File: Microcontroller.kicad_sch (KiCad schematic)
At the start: 17 parts, among them IC3 W25Q128JVSIQ, IC4 ESP32-S3R8, Q1 40MHz

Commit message: test 4
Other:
- note removed: "test text"
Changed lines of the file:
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@@
-		)
-	)
-	(text "test text"
-		(exclude_from_sim no)
-		(at 45.72 163.83 0)
-		(effects
-			(font
-				(size 1.27 1.27)
-			)
 		)
 	)

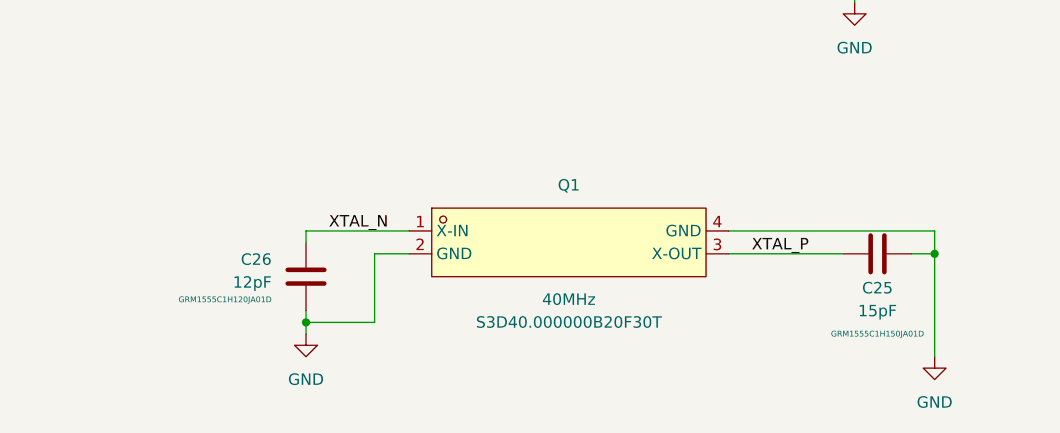
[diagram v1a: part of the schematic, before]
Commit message: Crystal Change
Crystal changed from active (CMSO) to passive with 2x 15pF load capacitors
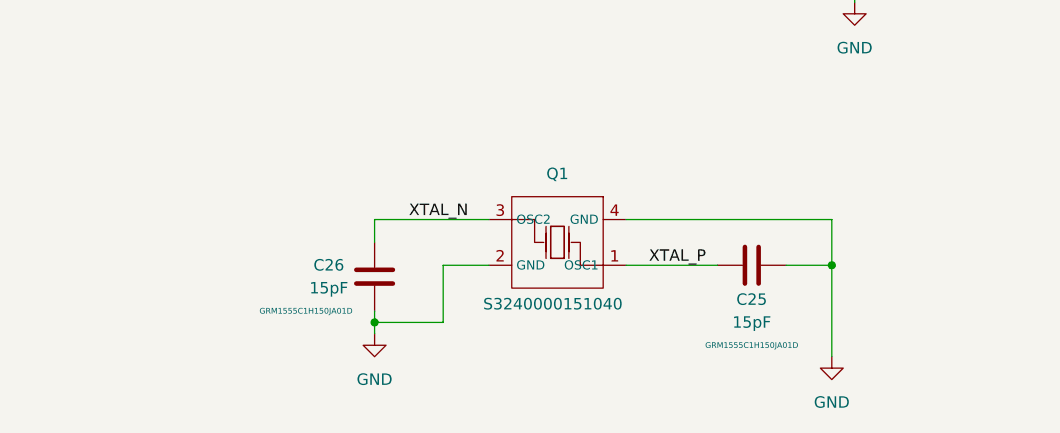
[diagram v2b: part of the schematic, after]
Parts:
- removed C26: 12pF, GRM1555C1H120JA01D:CAPC1005X55N, symbol Project Capacitors:CC0402KRX7R7BB104_1
- removed Q1: 40MHz, S3D40.000000B20F30T:OSC-SMD_4P-L3.2-W2.5-BL-1, symbol S3D40.000000B20F30T:S3D40.000000B20F30T
- added C26: 15pF, GRM1555C1H150JA01D:CAPC1005X55N, symbol Project Capacitors:GRM1555C1H150JA01D
- added Q1: 40MHz, S3240000151040:CRYSTAL-SMD_4P-L3.2-W2.5-BL, symbol S3240000151040:S3240000151040
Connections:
- net GND: now also C26.2, Q1.2 (GND), Q1.4 (GND)
- net XTAL_N: now also C26.1, Q1.3 (OSC2)
- net XTAL_P: now also Q1.1 (OSC1)
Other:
- moved on the sheet: C25
